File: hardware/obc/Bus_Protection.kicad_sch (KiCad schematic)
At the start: 44 parts, among them Q11 MMDT2907, Q12 BSS138DWQ-7, Q13 BSS138DWQ-7, Q15 MBT2222ADW1T1, Q16 MBT2222ADW1T1, Q18 BSS138DWQ-7, Q19 BSS138DWQ-7, Q7 MBT2222ADW1T1, Q8 MBT2222ADW1T1

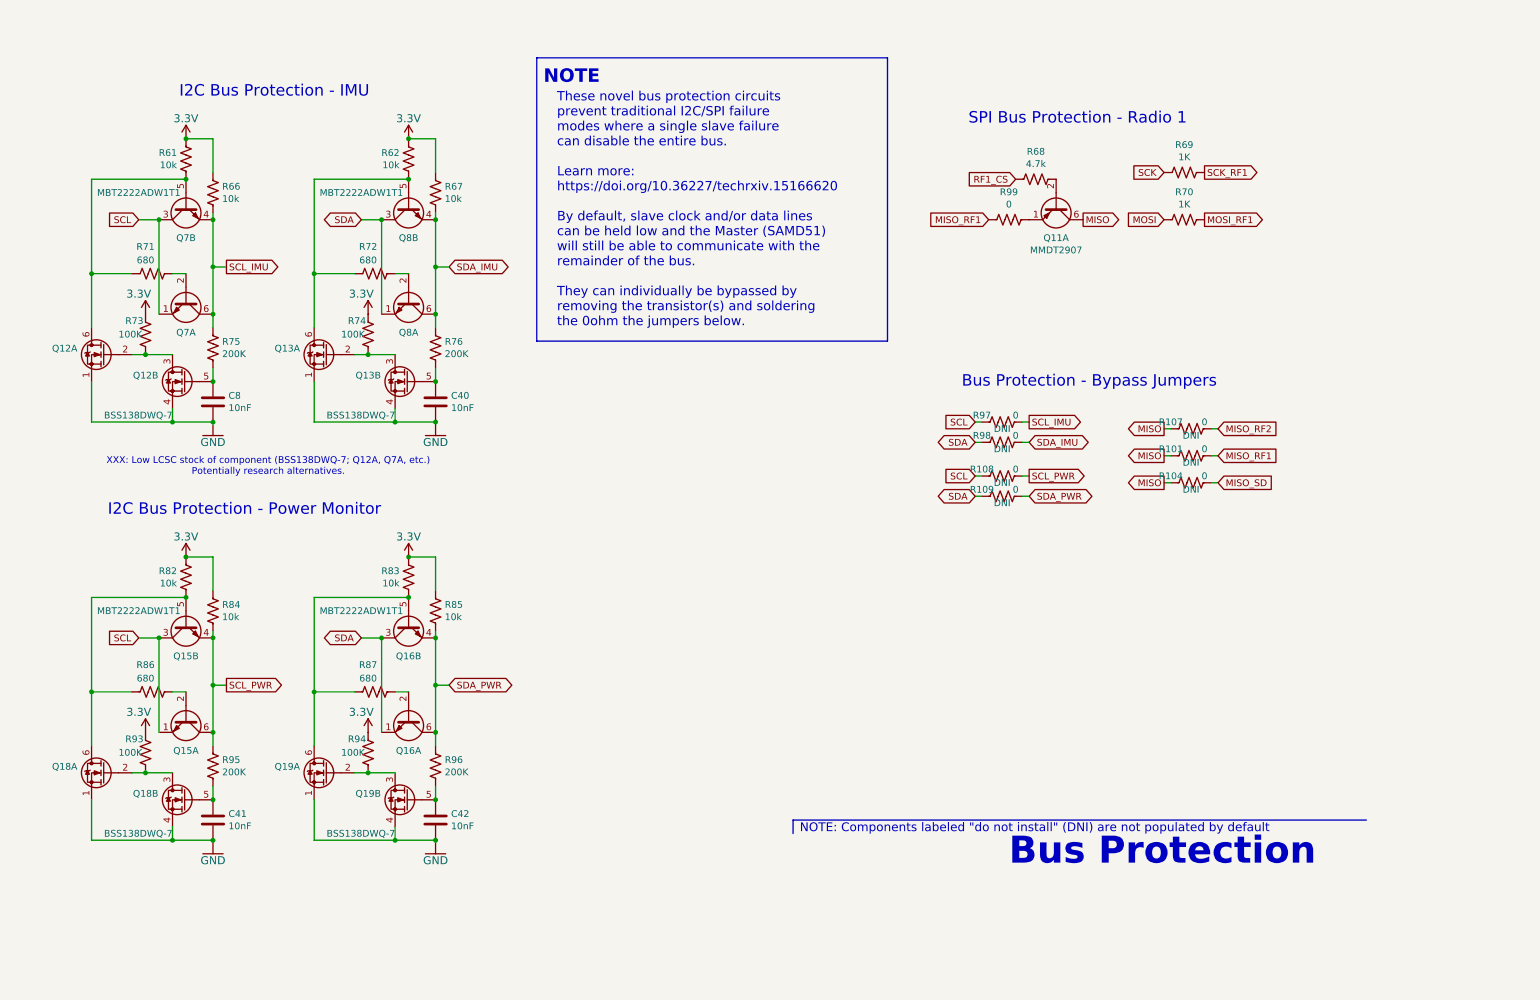
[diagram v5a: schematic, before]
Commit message: obc: footprint editing and schematic revision
Added GPS21+ and edited inductor footprints. Edited schematic circuitry and re-annotated schematic components.
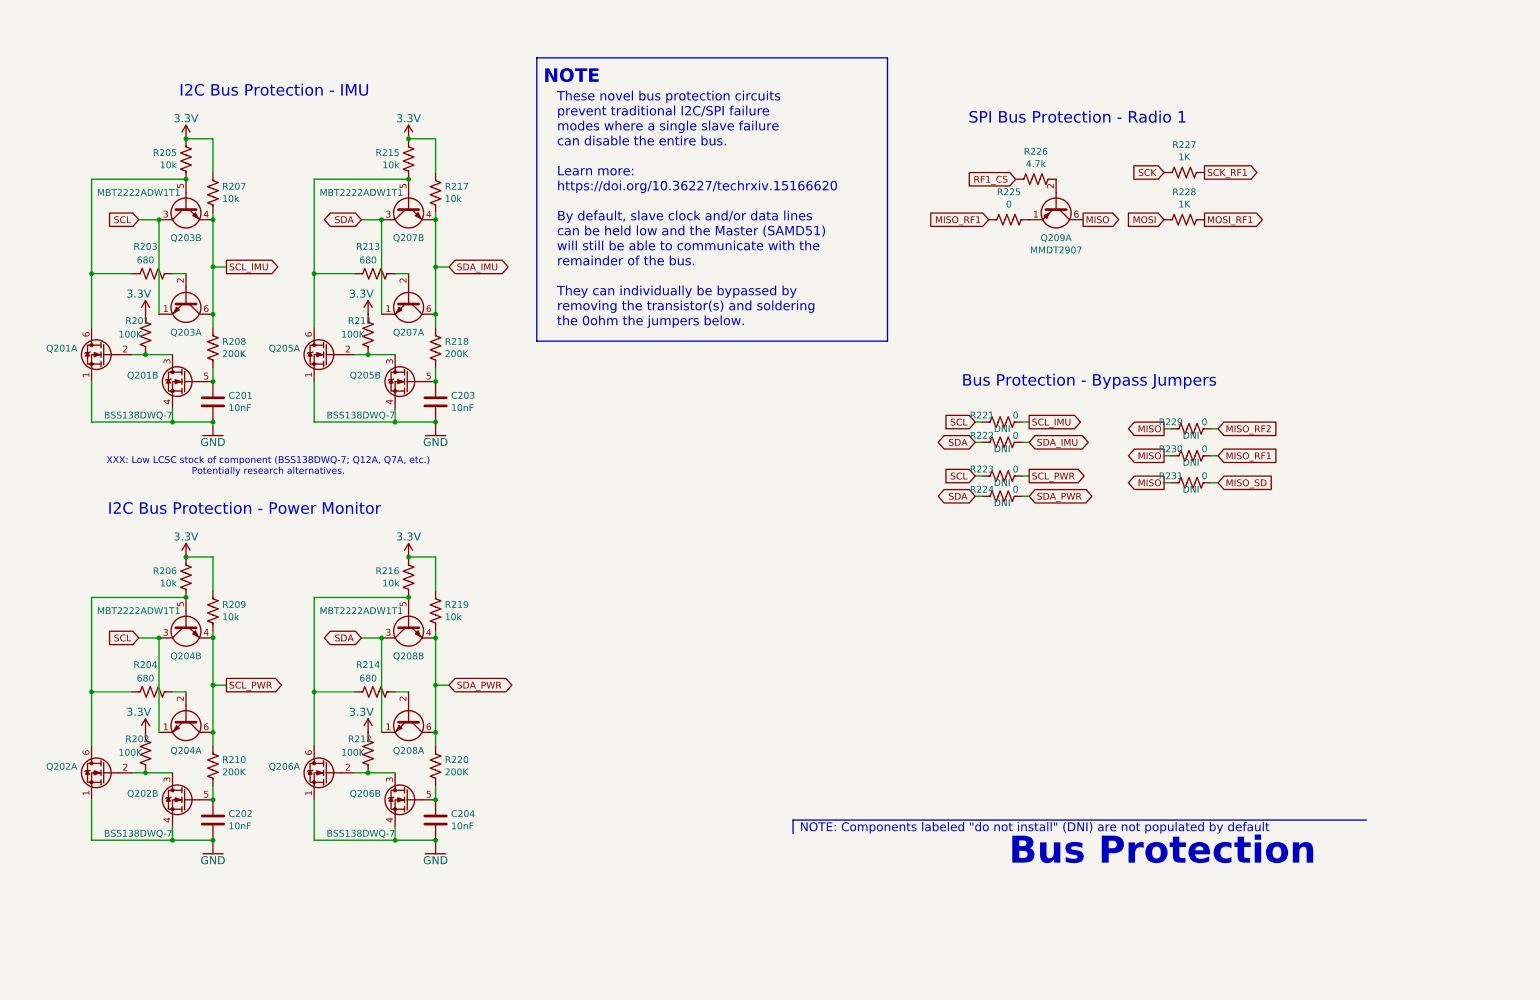
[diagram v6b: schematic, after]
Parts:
- renumbered C8 to C201, C41 to C202, C40 to C203, C42 to C204, Q12 to Q201, Q18 to Q202, Q7 to Q203, Q15 to Q204, Q13 to Q205, Q19 to Q206, Q8 to Q207, Q16 to Q208, Q11 to Q209, R73 to R201, R93 to R202, R71 to R203, R86 to R204, R61 to R205, R82 to R206, R66 to R207, R75 to R208, R84 to R209, R95 to R210, R74 to R211, R94 to R212, R72 to R213, R87 to R214, R62 to R215, R83 to R216, R67 to R217, R76 to R218, R85 to R219, R96 to R220, R97 to R221, R98 to R222, R108 to R223, R109 to R224, R99 to R225, R68 to R226, R69 to R227, R70 to R228, R107 to R229, R101 to R230, R104 to R231

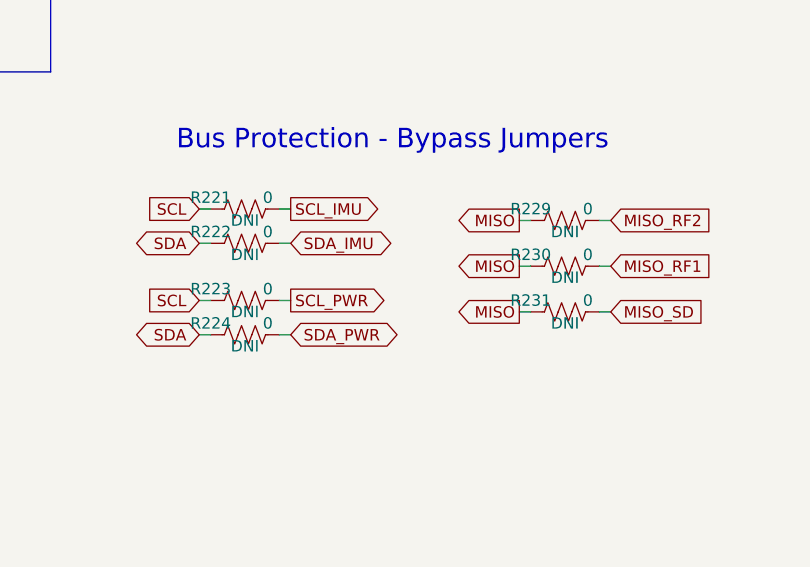
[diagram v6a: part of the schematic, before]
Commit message: obc: BOM editing
Edited the DNI status of several components to be more reflective of our obc setup plans.
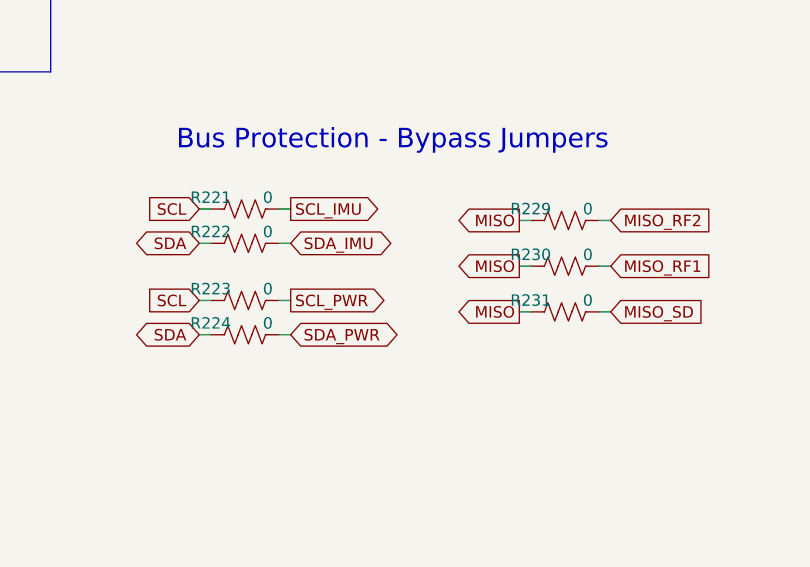
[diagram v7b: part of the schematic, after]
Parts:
- R221, R222, R223, R224, R229, R230, R231: DNI DNI -> (none); LCSC C2654002 -> (none)
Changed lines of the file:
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@@
 			)
 		)
-		(property "DNI" "DNI"
+		(property "DNI" ""
 			(at 199.39 109.22 90)
 			(effects
@@
 			)
 		)
-		(property "LCSC" "C2654002"
+		(property "LCSC" ""
 			(at 199.39 107.95 0)
 			(effects
@@
 			)
 		)
-		(property "DNI" "DNI"
+		(property "DNI" ""
 			(at 199.39 95.25 90)
 			(effects
@@
 			)
 		)
-		(property "LCSC" "C2654002"
+		(property "LCSC" ""
 			(at 199.39 93.98 0)
 			(effects
@@
 			)
 		)
-		(property "DNI" "DNI"
+		(property "DNI" ""
 			(at 199.39 99.06 90)
 			(effects
@@
 			)
 		)
-		(property "LCSC" "C2654002"
+		(property "LCSC" ""
 			(at 199.39 97.79 0)
 			(effects
@@
 			)
 		)
-		(property "DNI" "DNI"
+		(property "DNI" ""
 			(at 234.95 101.6 90)
 			(effects
@@
 			)
 		)
-		(property "LCSC" "C2654002"
+		(property "LCSC" ""
 			(at 234.95 100.33 0)
 			(effects
@@
 			)
 		)
-		(property "DNI" "DNI"
+		(property "DNI" ""
 			(at 234.95 106.68 90)
 			(effects
@@
 			)
 		)
-		(property "LCSC" "C2654002"
+		(property "LCSC" ""
 			(at 234.95 105.41 0)
 			(effects
@@
 			)
 		)
-		(property "DNI" "DNI"
+		(property "DNI" ""
 			(at 199.39 105.41 90)
 			(effects
@@
 			)
 		)
-		(property "LCSC" "C2654002"
+		(property "LCSC" ""
 			(at 199.39 104.14 0)
 			(effects
@@
 			)
 		)
-		(property "DNI" "DNI"
+		(property "DNI" ""
 			(at 234.95 96.52 90)
 			(effects
@@
 			)
 		)
-		(property "LCSC" "C2654002"
+		(property "LCSC" ""
 			(at 234.95 95.25 0)
 			(effects

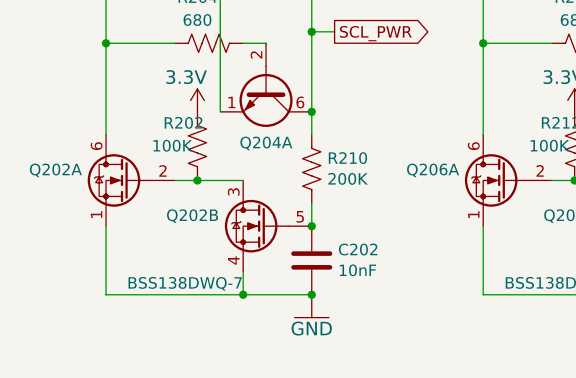
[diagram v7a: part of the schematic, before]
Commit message: obc: preliminary board layout
Entered design rules and grouped components according to schematic. Slightly edited BOM.
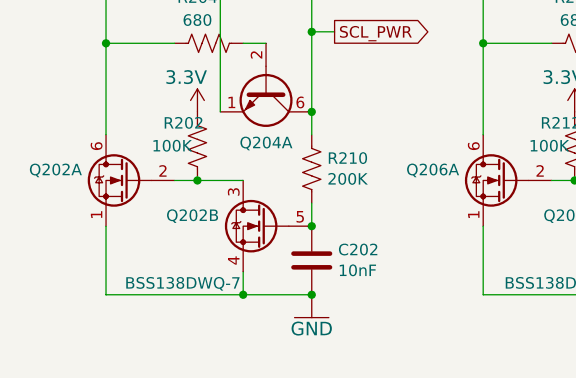
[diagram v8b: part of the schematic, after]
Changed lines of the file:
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@@
 		)
 		(property "Value" "BSS138DWQ-7"
-			(at 43.18 171.45 0)
+			(at 42.926 171.45 0)
 			(effects
 				(font
